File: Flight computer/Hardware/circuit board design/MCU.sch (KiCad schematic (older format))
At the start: 31 parts, among them J1 Conn_01x05, J8 Conn_01x04, U11 ATSAML21J18B-AUT, U7 W74M64FV, Y3 16MHz

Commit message: added in molex usb 3D cad and silk screen ICSS logo
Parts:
- added R4, R8: 1K, Resistor_SMD:R_0603_1608Metric, symbol Device:R
- J8: footprint Connector_PinHeader_2.54mm:PinHeader_1x05_P2.54mm_Vertical -> Connector_PinHeader_2.54mm:PinHeader_1x02_P2.54mm_Vertical; symbol Connector_Generic:Conn_01x04 -> Connector_Generic:Conn_01x02
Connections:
- net +3V3: now also R4.1, R8.1
- net at U11.10 (PB07): now also J8.2 (Pin_2), R8.2; no longer J8.4 (Pin_4)
- net at U11.5 (PB04): no longer J8.1 (Pin_1)
- net at U11.6 (PB05): no longer J8.2 (Pin_2)
- net at U11.9 (PB06): now also J8.1 (Pin_1), R4.2; no longer J8.3 (Pin_3)
- no-connect marks 8 -> 10
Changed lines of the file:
@@
 NoConn ~ 5100 4700
 $Comp
-L Connector_Generic:Conn_01x04 J8
+L Connector_Generic:Conn_01x02 J8
 U 1 1 5DB0330A
-P 8650 3800
-F 0 "J8" H 8730 3792 50  0000 L CNN
-F 1 "Conn_01x04" H 8730 3701 50  0000 L CNN
-F 2 "Connector_PinHeader_2.54mm:PinHeader_1x05_P2.54mm_Vertical" H 8650 3800 50  0001 C CNN
-F 3 "~" H 8650 3800 50  0001 C CNN
-	1    8650 3800
+P 8650 3900
+F 0 "J8" H 8730 3892 50  0000 L CNN
+F 1 "Conn_01x04" H 8730 3801 50  0000 L CNN
+F 2 "Connector_PinHeader_2.54mm:PinHeader_1x02_P2.54mm_Vertical" H 8650 3900 50  0001 C CNN
+F 3 "~" H 8650 3900 50  0001 C CNN
+	1    8650 3900
 	1    0    0    -1
 $EndComp
@@
 	1    0    0    -1
 $EndComp
+NoConn ~ 7100 3800
+NoConn ~ 7100 3700
+$Comp
+L power:+3.3V #PWR034
+U 1 1 5DB6F8DB
+P 8250 3400
+F 0 "#PWR034" H 8250 3250 50  0001 C CNN
+F 1 "+3.3V" H 8265 3573 50  0000 C CNN
+F 2 "" H 8250 3400 50  0001 C CNN
+F 3 "" H 8250 3400 50  0001 C CNN
+	1    8250 3400
+	1    0    0    -1
+$EndComp
+$Comp
+L power:+3.3V #PWR017
+U 1 1 5DB96344
+P 8000 3400
+F 0 "#PWR017" H 8000 3250 50  0001 C CNN
+F 1 "+3.3V" H 8015 3573 50  0000 C CNN
+F 2 "" H 8000 3400 50  0001 C CNN
+F 3 "" H 8000 3400 50  0001 C CNN
+	1    8000 3400
+	1    0    0    -1
+$EndComp
 Wire Wire Line
-	7100 3700 8450 3700
+	8250 4000 8450 4000
+Connection ~ 8250 4000
 Wire Wire Line
-	8450 3800 7100 3800
+	7100 4000 8250 4000
+$Comp
+L Device:R R8
+U 1 1 5DB65E3A
+P 8250 3650
+F 0 "R8" H 8320 3696 50  0000 L CNN
+F 1 "1K" H 8320 3605 50  0000 L CNN
+F 2 "Resistor_SMD:R_0603_1608Metric" V 8180 3650 50  0001 C CNN
+F 3 "~" H 8250 3650 50  0001 C CNN
+	1    8250 3650
+	-1   0    0    -1
+$EndComp
 Wire Wire Line
-	7100 3900 8450 3900
+	8250 3500 8250 3400
 Wire Wire Line
-	7100 4000 8450 4000
+	8250 4000 8250 3800
+Wire Wire Line
+	8000 3900 8450 3900
+Connection ~ 8000 3900
+Wire Wire Line
+	7100 3900 8000 3900
+$Comp
+L Device:R R4
+U 1 1 5DB6561B
+P 8000 3650
+F 0 "R4" H 8070 3696 50  0000 L CNN
+F 1 "1K" H 8070 3605 50  0000 L CNN
+F 2 "Resistor_SMD:R_0603_1608Metric" V 7930 3650 50  0001 C CNN
+F 3 "~" H 8000 3650 50  0001 C CNN
+	1    8000 3650
+	-1   0    0    -1
+$EndComp
+Wire Wire Line
+	8000 3900 8000 3800
+Wire Wire Line
+	8000 3500 8000 3400
 $EndSCHEMATC

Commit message: done for today
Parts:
- removed J8: Conn_01x04, Connector_PinHeader_2.54mm:PinHeader_1x02_P2.54mm_Vertical, symbol Connector_Generic:Conn_01x02
- removed R4, R8: 1K, Resistor_SMD:R_0603_1608Metric, symbol Device:R
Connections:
- no-connect marks 10 -> 12
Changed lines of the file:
@@
 NoConn ~ 5100 4700
-$Comp
-L Connector_Generic:Conn_01x02 J8
-U 1 1 5DB0330A
-P 8650 3900
-F 0 "J8" H 8730 3892 50  0000 L CNN
-F 1 "Conn_01x04" H 8730 3801 50  0000 L CNN
-F 2 "Connector_PinHeader_2.54mm:PinHeader_1x02_P2.54mm_Vertical" H 8650 3900 50  0001 C CNN
-F 3 "~" H 8650 3900 50  0001 C CNN
-	1    8650 3900
-	1    0    0    -1
-$EndComp
 $Comp
 L MCU_Microchip_SAML:ATSAML21J18B-AUT U11
@@
 NoConn ~ 7100 3800
 NoConn ~ 7100 3700
-$Comp
-L power:+3.3V #PWR034
-U 1 1 5DB6F8DB
-P 8250 3400
-F 0 "#PWR034" H 8250 3250 50  0001 C CNN
-F 1 "+3.3V" H 8265 3573 50  0000 C CNN
-F 2 "" H 8250 3400 50  0001 C CNN
-F 3 "" H 8250 3400 50  0001 C CNN
-	1    8250 3400
-	1    0    0    -1
-$EndComp
-$Comp
-L power:+3.3V #PWR017
-U 1 1 5DB96344
-P 8000 3400
-F 0 "#PWR017" H 8000 3250 50  0001 C CNN
-F 1 "+3.3V" H 8015 3573 50  0000 C CNN
-F 2 "" H 8000 3400 50  0001 C CNN
-F 3 "" H 8000 3400 50  0001 C CNN
-	1    8000 3400
-	1    0    0    -1
-$EndComp
-Wire Wire Line
-	8250 4000 8450 4000
-Connection ~ 8250 4000
-Wire Wire Line
-	7100 4000 8250 4000
-$Comp
-L Device:R R8
-U 1 1 5DB65E3A
-P 8250 3650
-F 0 "R8" H 8320 3696 50  0000 L CNN
-F 1 "1K" H 8320 3605 50  0000 L CNN
-F 2 "Resistor_SMD:R_0603_1608Metric" V 8180 3650 50  0001 C CNN
-F 3 "~" H 8250 3650 50  0001 C CNN
-	1    8250 3650
-	-1   0    0    -1
-$EndComp
-Wire Wire Line
-	8250 3500 8250 3400
-Wire Wire Line
-	8250 4000 8250 3800
-Wire Wire Line
-	8000 3900 8450 3900
-Connection ~ 8000 3900
-Wire Wire Line
-	7100 3900 8000 3900
-$Comp
-L Device:R R4
-U 1 1 5DB6561B
-P 8000 3650
-F 0 "R4" H 8070 3696 50  0000 L CNN
-F 1 "1K" H 8070 3605 50  0000 L CNN
-F 2 "Resistor_SMD:R_0603_1608Metric" V 7930 3650 50  0001 C CNN
-F 3 "~" H 8000 3650 50  0001 C CNN
-	1    8000 3650
-	-1   0    0    -1
-$EndComp
-Wire Wire Line
-	8000 3900 8000 3800
-Wire Wire Line
-	8000 3500 8000 3400
+NoConn ~ 7100 4000
+NoConn ~ 7100 3900
 $EndSCHEMATC

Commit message: Finished routing the board with 3.3V power plane
Power for mosfets comes from 2mm tracks on top layer. Todo: make their connection to ground more robust
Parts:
- Y3: footprint Crystal:Crystal_SMD_2520-4Pin_2.5x2.0mm -> flight-computer:Crystal_SMD_2520-4Pin_2.5x2.0mm
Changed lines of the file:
@@
 F 0 "Y3" H 3300 4850 50  0000 C CNN
 F 1 "16MHz" H 3300 4950 50  0000 C CNN
-F 2 "Crystal:Crystal_SMD_2520-4Pin_2.5x2.0mm" H 3300 4400 50  0001 C CNN
+F 2 "flight-computer:Crystal_SMD_2520-4Pin_2.5x2.0mm" H 3300 4400 50  0001 C CNN
 F 3 "https://docs-emea.rs-online.com/webdocs/15dc/0900766b815dc75d.pdf" H 3300 4400 50  0001 C CNN
 	1    3300 4400

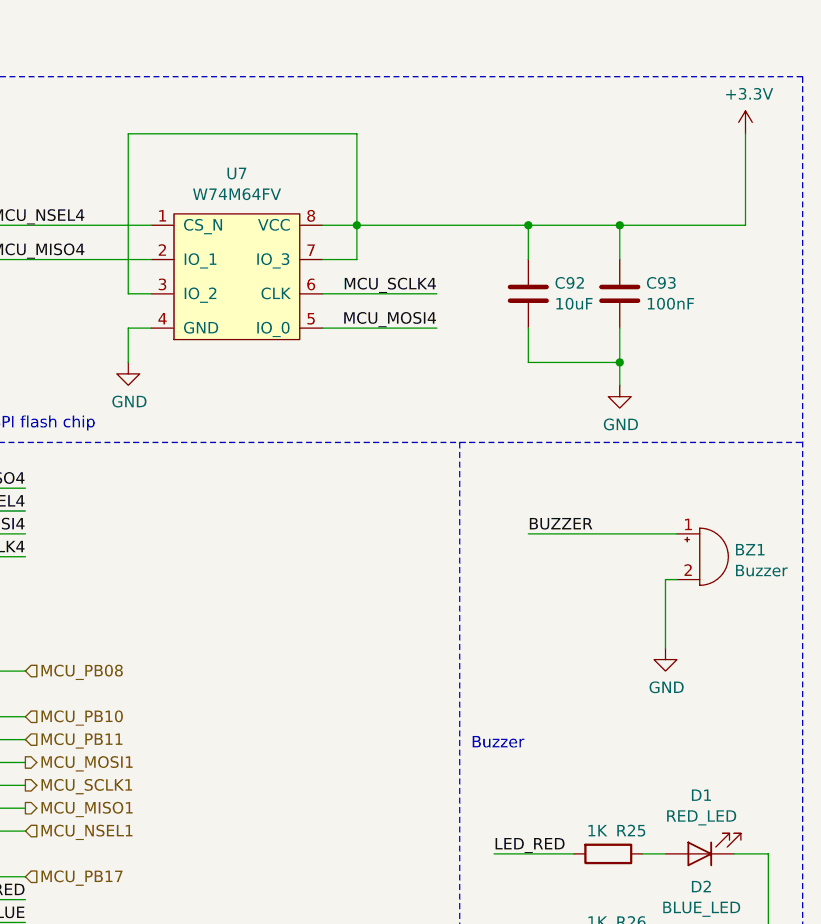
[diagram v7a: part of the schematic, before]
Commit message: changed SPI flash chip
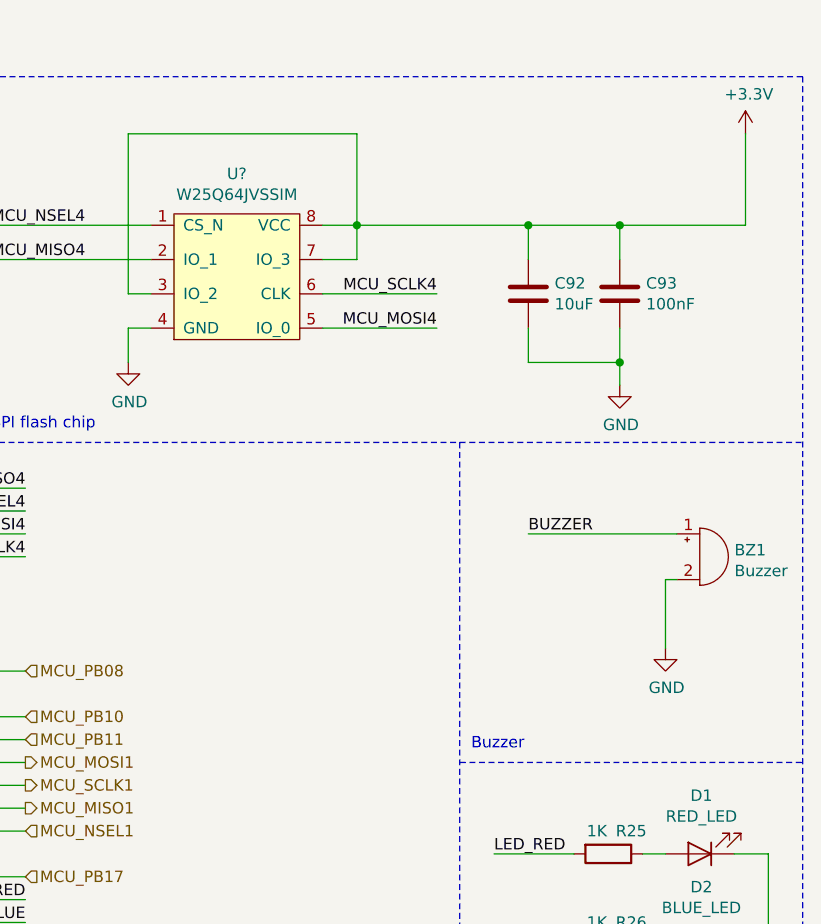
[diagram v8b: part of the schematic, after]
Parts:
- removed U7: W74M64FV, Package_SO:SOIC-8_5.23x5.23mm_P1.27mm, symbol flight-computer:W74M64FV
- added U?: W25Q64JVSSIM, Package_SO:SOIC-8_5.23x5.23mm_P1.27mm, symbol flight-computer:W25Q64JVSSIM
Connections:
- net +3V3: now also U?.3 (IO_2), U?.7 (IO_3), U?.8 (VCC)
- net GND: now also U?.4 (GND)
- net MCU_MISO4: now also U?.2 (IO_1)
- net MCU_MOSI4: now also U?.5 (IO_0)
- net MCU_NSEL4: now also U?.1 (CS_N)
- net MCU_SCLK4: now also U?.6 (CLK)
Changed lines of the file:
@@
-$EndComp
-$Comp
-L flight-computer:W74M64FV U7
-U 1 1 5D77FBCE
-P 8300 2650
-F 0 "U7" H 8575 3375 50  0000 C CNN
-F 1 "W74M64FV" H 8575 3284 50  0000 C CNN
-F 2 "Package_SO:SOIC-8_5.23x5.23mm_P1.27mm" H 8300 2650 50  0001 C CNN
-F 3 "https://docs-emea.rs-online.com/webdocs/1623/0900766b81623058.pdf" H 8300 2650 50  0001 C CNN
-F 4 "https://www.mouser.co.uk/ProductDetail/Winbond/W74M64FVSSIQ?qs=qSfuJ%252Bfl%2Fd52YBej%252Bs3iEg==" H 8300 2650 50  0001 C CNN "Purchase link"
-	1    8300 2650
-	1    0    0    -1
 $EndComp
 $Comp
@@
 NoConn ~ 7100 4000
 NoConn ~ 7100 3900
+Wire Notes Line
+	9550 4500 11050 4500
+$Comp
+L flight-computer:W25Q64JVSSIM U?
+U 1 1 5D850B8A
+P 8300 2650
+F 0 "U?" H 8575 3375 50  0000 C CNN
+F 1 "W25Q64JVSSIM" H 8575 3284 50  0000 C CNN
+F 2 "Package_SO:SOIC-8_5.23x5.23mm_P1.27mm" H 8300 2650 50  0001 C CNN
+F 3 "https://docs-emea.rs-online.com/webdocs/1703/0900766b81703f87.pdf" H 8300 2650 50  0001 C CNN
+F 4 "https://uk.rs-online.com/web/p/flash-memory/1882666/" H 8300 2650 50  0001 C CNN "Purchase link"
+	1    8300 2650
+	1    0    0    -1
+$EndComp
 $EndSCHEMATC
